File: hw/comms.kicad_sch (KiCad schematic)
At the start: 13 parts, among them J7 CAN IN, J8 CAN OUT, J9 USB-C, SW1 TERM, U6 TCAN3413, U7 USBLC6-2SC6

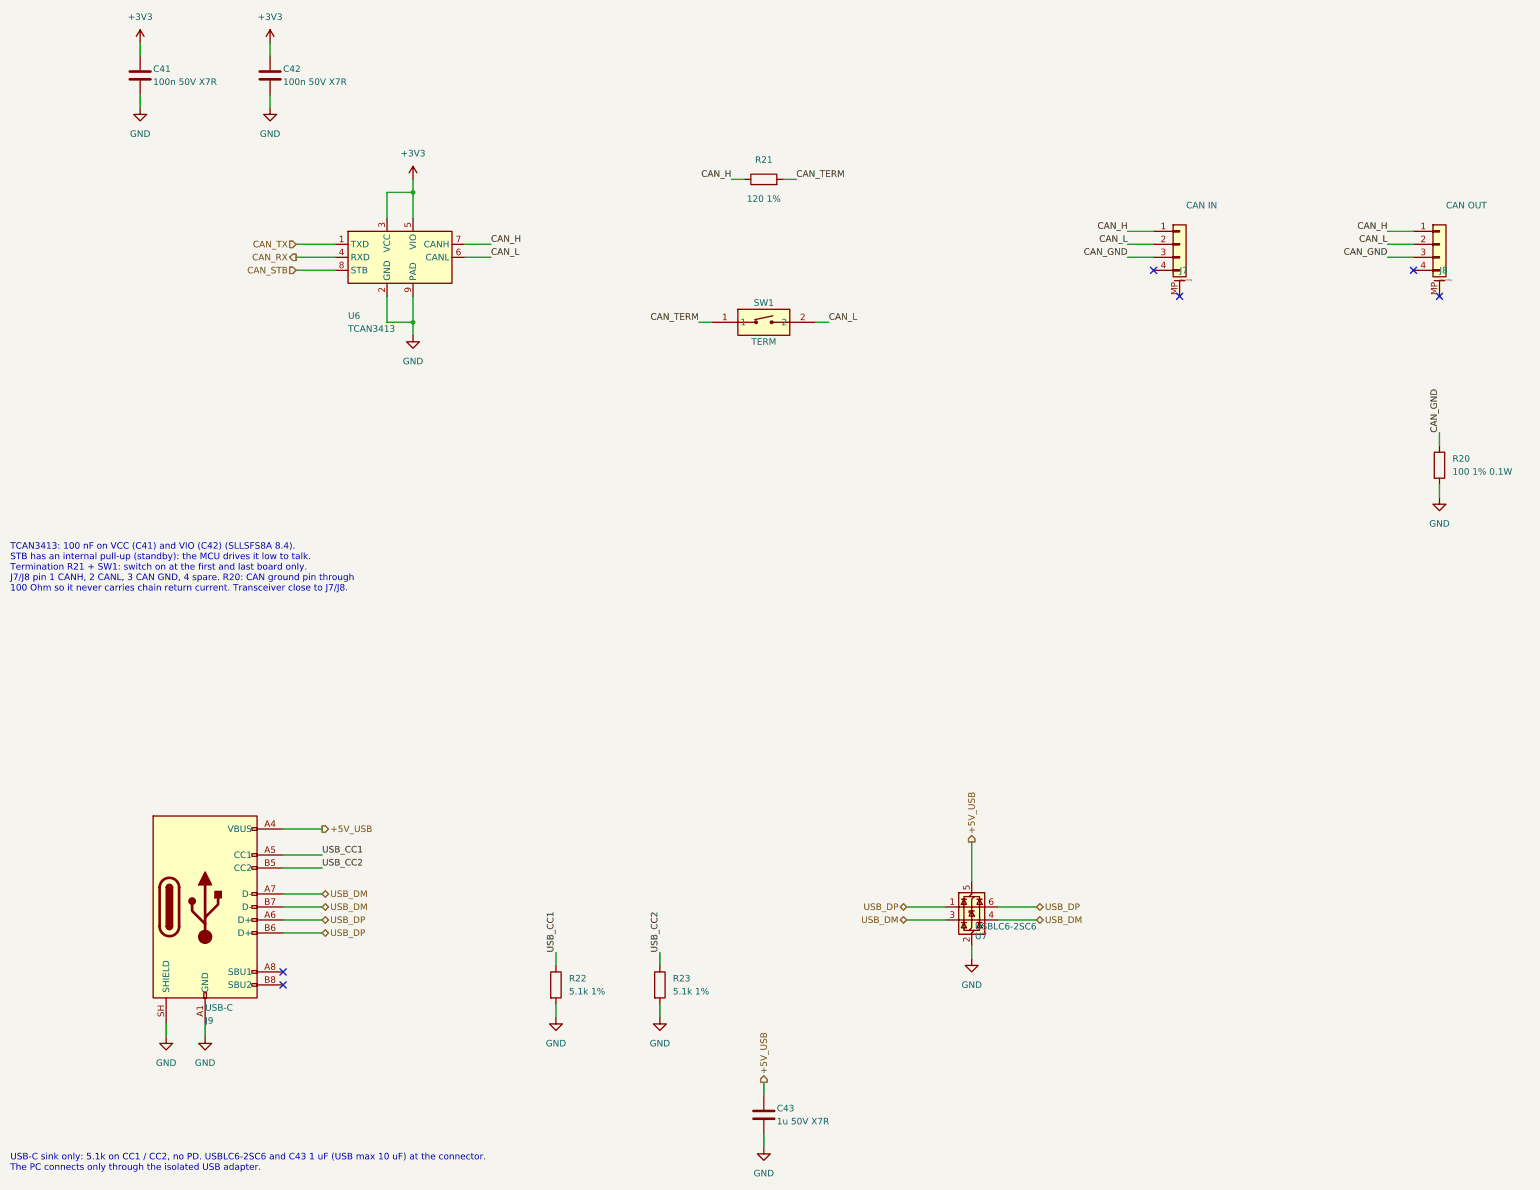
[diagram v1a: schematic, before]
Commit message: Apply schematic review fixes and connector changes
- Remove the RC snubber pads (ringing handled by layout and IDRIVE)
  and renumber R/C references to close the gap.
- CAN connectors: JST-GH 3-pin (CANH, CANL, GND).
- Power connectors: XT30PW-F female for both bus IN and OUT so the
  live side of every link is shrouded; polarity checked on a real
  part (pad 1 GND under the rounded end, pad 2 VBUS under the flat
  end). Male XT30 footprint, model and datasheet removed.
- AS5047P CSn 10k pull-up so encoder inputs never float while the
  MCU is in reset or ROM DFU.
- LM5008A RT 180k -> 240k: on-time stays >= 400 ns at 54 V across
  the TON spread.
- Every BOM line checked in stock against JLCPCB's assembly library.
- Kelvin-tap placement added to the layout rules.

Co-Authored-By: Claude Opus 5.5 <noreply@anthropic.com>
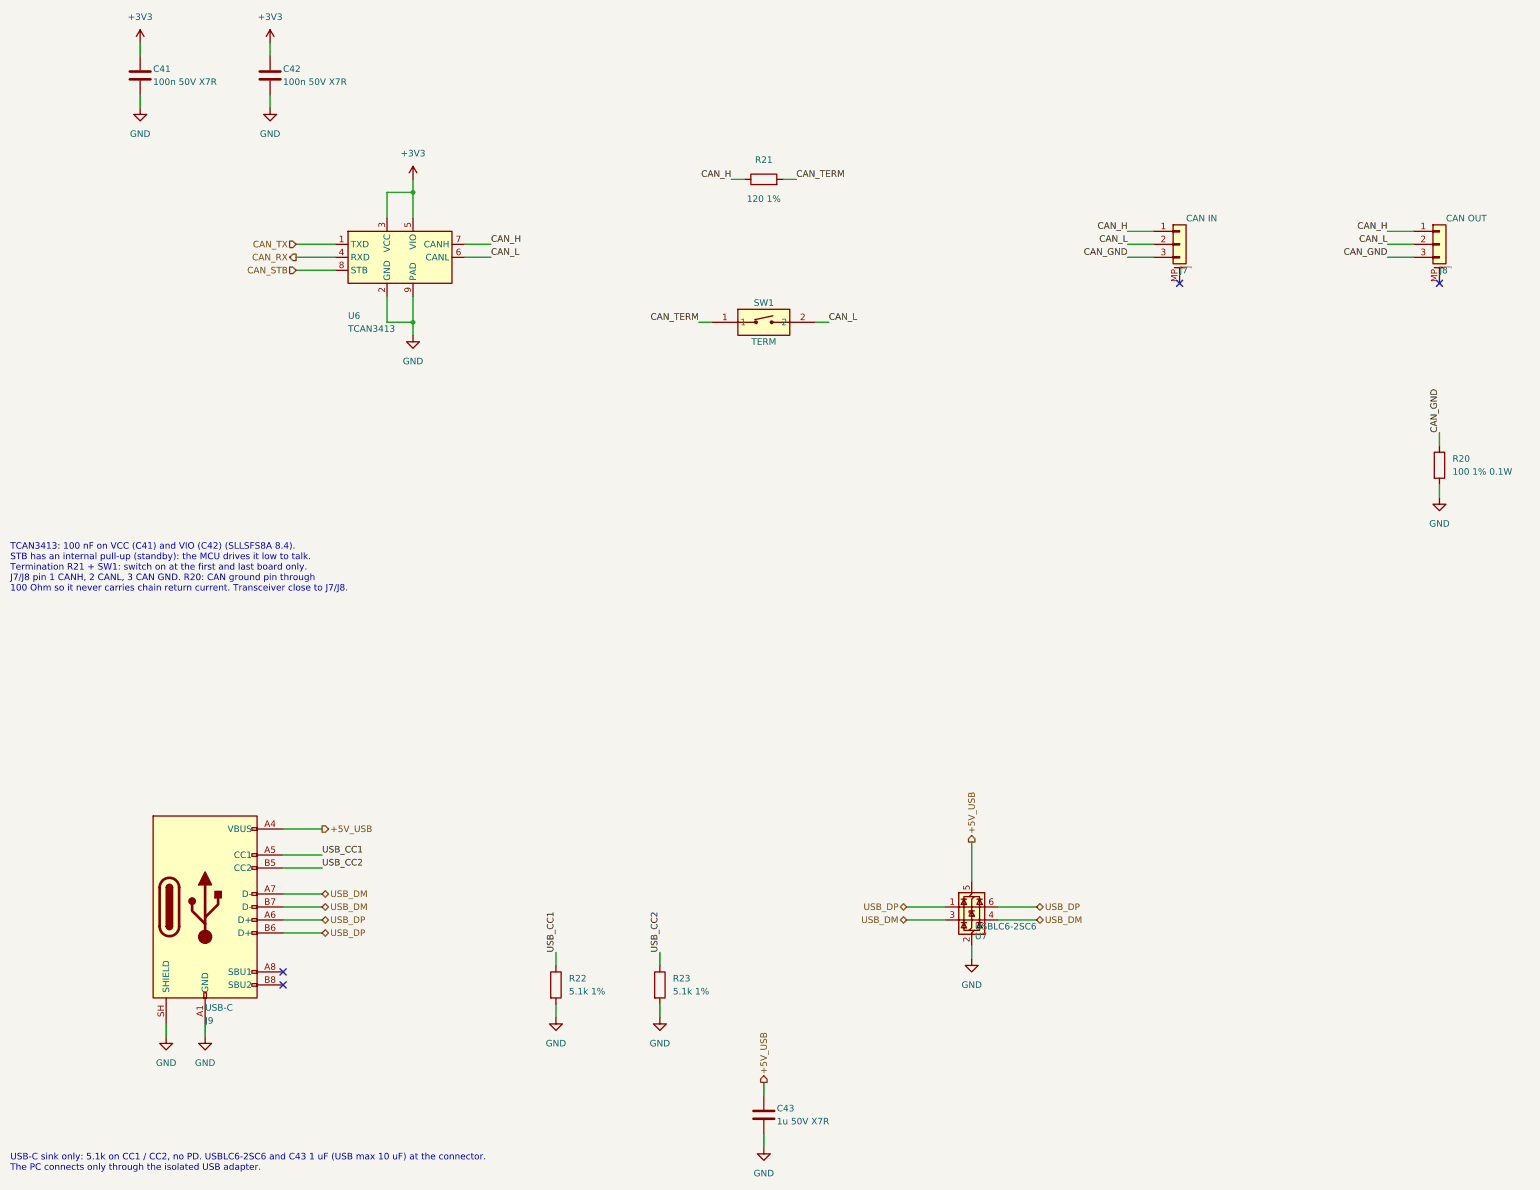
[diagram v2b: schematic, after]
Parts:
- removed J7: CAN IN, Connector_JST:JST_GH_SM04B-GHS-TB_1x04-1MP_P1.25mm_Horizontal, symbol Connector_Generic_MountingPin:Conn_01x04_MountingPin
- removed J8: CAN OUT, Connector_JST:JST_GH_SM04B-GHS-TB_1x04-1MP_P1.25mm_Horizontal, symbol Connector_Generic_MountingPin:Conn_01x04_MountingPin
- added J7: CAN IN, Connector_JST:JST_GH_SM03B-GHS-TB_1x03-1MP_P1.25mm_Horizontal, symbol Connector_Generic_MountingPin:Conn_01x03_MountingPin
- added J8: CAN OUT, Connector_JST:JST_GH_SM03B-GHS-TB_1x03-1MP_P1.25mm_Horizontal, symbol Connector_Generic_MountingPin:Conn_01x03_MountingPin
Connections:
- net CAN_GND: now also J7.3 (Pin_3), J8.3 (Pin_3)
- net CAN_H: now also J7.1 (Pin_1), J8.1 (Pin_1)
- net CAN_L: now also J7.2 (Pin_2), J8.2 (Pin_2)
- no-connect marks 6 -> 4
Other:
- note added: "TCAN3413: 100 nF on VCC (C41) and VIO (C42) (SLLSFS8A 8.4). STB has an internal pull-up (standby): the MCU drives it low to talk. Termination R21 + SW1: switch on at the first and last board only. J7/J8 pin 1 CANH, 2 CANL, 3 CAN GND. R20: CAN ground pin through 100 Ohm so it never carries chain return current. Transceiver close to J7/J8."
- note removed: "TCAN3413: 100 nF on VCC (C41) and VIO (C42) (SLLSFS8A 8.4). STB has an internal pull-up (standby): the MCU drives it low to talk. Termination R21 + SW1: switch on at the first and last board only. J7/J8 pin 1 CANH, 2 CANL, 3 CAN GND, 4 spare. R20: CAN ground pin through 100 Ohm so it never carries chain return current. Transceiver close to J7/J8."
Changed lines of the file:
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@@
 		(instances
 			(project "comms"
-				(path "/23e15ccf-2162-4caa-a05b-71e788486361/49fa0cbe-12ed-4e3b-b7f4-bb953e26e881"
+				(path "/dc3b1c6f-161a-46e4-9985-32c8fd205458/54234469-6ff5-4cf8-9289-b79c93d7bfe3"
 					(reference "U6")
 					(unit 1)
@@
 		(instances
 			(project "comms"
-				(path "/23e15ccf-2162-4caa-a05b-71e788486361/49fa0cbe-12ed-4e3b-b7f4-bb953e26e881"
+				(path "/dc3b1c6f-161a-46e4-9985-32c8fd205458/54234469-6ff5-4cf8-9289-b79c93d7bfe3"
 					(reference "#PWRCOM01")
 					(unit 1)
@@
 		(instances
 			(project "comms"
-				(path "/23e15ccf-2162-4caa-a05b-71e788486361/49fa0cbe-12ed-4e3b-b7f4-bb953e26e881"
+				(path "/dc3b1c6f-161a-46e4-9985-32c8fd205458/54234469-6ff5-4cf8-9289-b79c93d7bfe3"
 					(reference "#PWRCOM02")
 					(unit 1)
@@
 		(instances
 			(project "comms"
-				(path "/23e15ccf-2162-4caa-a05b-71e788486361/49fa0cbe-12ed-4e3b-b7f4-bb953e26e881"
+				(path "/dc3b1c6f-161a-46e4-9985-32c8fd205458/54234469-6ff5-4cf8-9289-b79c93d7bfe3"
 					(reference "C41")
 					(unit 1)
@@
 		(instances
 			(project "comms"
-				(path "/23e15ccf-2162-4caa-a05b-71e788486361/49fa0cbe-12ed-4e3b-b7f4-bb953e26e881"
+				(path "/dc3b1c6f-161a-46e4-9985-32c8fd205458/54234469-6ff5-4cf8-9289-b79c93d7bfe3"
 					(reference "#PWRCOM03")
 					(unit 1)
@@
 		(instances
 			(project "comms"
-				(path "/23e15ccf-2162-4caa-a05b-71e788486361/49fa0cbe-12ed-4e3b-b7f4-bb953e26e881"
+				(path "/dc3b1c6f-161a-46e4-9985-32c8fd205458/54234469-6ff5-4cf8-9289-b79c93d7bfe3"
 					(reference "#PWRCOM04")
 					(unit 1)
@@
 		(instances
 			(project "comms"
-				(path "/23e15ccf-2162-4caa-a05b-71e788486361/49fa0cbe-12ed-4e3b-b7f4-bb953e26e881"
+				(path "/dc3b1c6f-161a-46e4-9985-32c8fd205458/54234469-6ff5-4cf8-9289-b79c93d7bfe3"
 					(reference "C42")
 					(unit 1)
@@
 		(instances
 			(project "comms"
-				(path "/23e15ccf-2162-4caa-a05b-71e788486361/49fa0cbe-12ed-4e3b-b7f4-bb953e26e881"
+				(path "/dc3b1c6f-161a-46e4-9985-32c8fd205458/54234469-6ff5-4cf8-9289-b79c93d7bfe3"
 					(reference "#PWRCOM05")
 					(unit 1)
@@
 		(instances
 			(project "comms"
-				(path "/23e15ccf-2162-4caa-a05b-71e788486361/49fa0cbe-12ed-4e3b-b7f4-bb953e26e881"
+				(path "/dc3b1c6f-161a-46e4-9985-32c8fd205458/54234469-6ff5-4cf8-9289-b79c93d7bfe3"
 					(reference "#PWRCOM06")
 					(unit 1)
@@
 		(instances
 			(project "comms"
-				(path "/23e15ccf-2162-4caa-a05b-71e788486361/49fa0cbe-12ed-4e3b-b7f4-bb953e26e881"
+				(path "/dc3b1c6f-161a-46e4-9985-32c8fd205458/54234469-6ff5-4cf8-9289-b79c93d7bfe3"
 					(reference "R21")
 					(unit 1)
@@
 		(instances
 			(project "comms"
-				(path "/23e15ccf-2162-4caa-a05b-71e788486361/49fa0cbe-12ed-4e3b-b7f4-bb953e26e881"
+				(path "/dc3b1c6f-161a-46e4-9985-32c8fd205458/54234469-6ff5-4cf8-9289-b79c93d7bfe3"
 					(reference "SW1")
 					(unit 1)
@@
 	)
 	(symbol
-		(lib_id "Connector_Generic_MountingPin:Conn_01x04_MountingPin")
+		(lib_id "Connector_Generic_MountingPin:Conn_01x03_MountingPin")
 		(at 254 83.82 0)
 		(unit 1)
@@
 		)
 		(property "Value" "CAN IN"
-			(at 255.27 76.2 0.0000)
-			(effects
-				(font
-					(size 1.27 1.27)
-				)
-				(justify left)
-			)
-		)
-		(property "Footprint" "Connector_JST:JST_GH_SM04B-GHS-TB_1x04-1MP_P1.25mm_Horizontal"
+			(at 255.27 78.74 0.0000)
+			(effects
+				(font
+					(size 1.27 1.27)
+				)
+				(justify left)
+			)
+		)
+		(property "Footprint" "Connector_JST:JST_GH_SM03B-GHS-TB_1x03-1MP_P1.25mm_Horizontal"
 			(at 254 83.82 0.0000)
 			(effects
@@
 			)
 		)
-		(property "LCSC" "C189895"
+		(property "LCSC" "C514175"
 			(at 256.54 88.8999 0)
 			(hide yes)
@@
 			)
 		)
-		(property "MPN" "SM04B-GHS-TB(LF)(SN)"
+		(property "MPN" "SM03B-GHS-TB(LF)(SN)"
 			(at 256.54 88.8999 0)
 			(hide yes)
@@
 		(pin "3"
 		)
-		(pin "4"
-		)
 		(pin "MP"
 		)
 		(instances
 			(project "comms"
-				(path "/23e15ccf-2162-4caa-a05b-71e788486361/49fa0cbe-12ed-4e3b-b7f4-bb953e26e881"
+				(path "/dc3b1c6f-161a-46e4-9985-32c8fd205458/54234469-6ff5-4cf8-9289-b79c93d7bfe3"
 					(reference "J7")
 					(unit 1)
@@
 	)
 	(symbol
-		(lib_id "Connector_Generic_MountingPin:Conn_01x04_MountingPin")
+		(lib_id "Connector_Generic_MountingPin:Conn_01x03_MountingPin")
 		(at 304.8 83.82 0)
 		(unit 1)
@@
 		)
 		(property "Value" "CAN OUT"
-			(at 306.07 76.2 0.0000)
-			(effects
-				(font
-					(size 1.27 1.27)
-				)
-				(justify left)
-			)
-		)
-		(property "Footprint" "Connector_JST:JST_GH_SM04B-GHS-TB_1x04-1MP_P1.25mm_Horizontal"
+			(at 306.07 78.74 0.0000)
+			(effects
+				(font
+					(size 1.27 1.27)
+				)
+				(justify left)
+			)
+		)
+		(property "Footprint" "Connector_JST:JST_GH_SM03B-GHS-TB_1x03-1MP_P1.25mm_Horizontal"
 			(at 304.8 83.82 0.0000)
 			(effects
@@
 			)
 		)
-		(property "LCSC" "C189895"
+		(property "LCSC" "C514175"
 			(at 307.34 88.8999 0)
 			(hide yes)
@@
 			)
 		)
-		(property "MPN" "SM04B-GHS-TB(LF)(SN)"
+		(property "MPN" "SM03B-GHS-TB(LF)(SN)"
 			(at 307.34 88.8999 0)
 			(hide yes)
@@
 		(pin "3"
 		)
-		(pin "4"
-		)
 		(pin "MP"
 		)
 		(instances
 			(project "comms"
-				(path "/23e15ccf-2162-4caa-a05b-71e788486361/49fa0cbe-12ed-4e3b-b7f4-bb953e26e881"
+				(path "/dc3b1c6f-161a-46e4-9985-32c8fd205458/54234469-6ff5-4cf8-9289-b79c93d7bfe3"
 					(reference "J8")
 					(unit 1)
@@
 		(instances
 			(project "comms"
-				(path "/23e15ccf-2162-4caa-a05b-71e788486361/49fa0cbe-12ed-4e3b-b7f4-bb953e26e881"
+				(path "/dc3b1c6f-161a-46e4-9985-32c8fd205458/54234469-6ff5-4cf8-9289-b79c93d7bfe3"
 					(reference "R20")
 					(unit 1)
@@
 		(instances
 			(project "comms"
-				(path "/23e15ccf-2162-4caa-a05b-71e788486361/49fa0cbe-12ed-4e3b-b7f4-bb953e26e881"
+				(path "/dc3b1c6f-161a-46e4-9985-32c8fd205458/54234469-6ff5-4cf8-9289-b79c93d7bfe3"
 					(reference "#PWRCOM07")
 					(unit 1)
@@
 		(instances
 			(project "comms"
-				(path "/23e15ccf-2162-4caa-a05b-71e788486361/49fa0cbe-12ed-4e3b-b7f4-bb953e26e881"
+				(path "/dc3b1c6f-161a-46e4-9985-32c8fd205458/54234469-6ff5-4cf8-9289-b79c93d7bfe3"
 					(reference "J9")
 					(unit 1)
@@
 		(instances
 			(project "comms"
-				(path "/23e15ccf-2162-4caa-a05b-71e788486361/49fa0cbe-12ed-4e3b-b7f4-bb953e26e881"
+				(path "/dc3b1c6f-161a-46e4-9985-32c8fd205458/54234469-6ff5-4cf8-9289-b79c93d7bfe3"
 					(reference "#PWRCOM08")
 					(unit 1)
@@
 		(instances
 			(project "comms"
-				(path "/23e15ccf-2162-4caa-a05b-71e788486361/49fa0cbe-12ed-4e3b-b7f4-bb953e26e881"
+				(path "/dc3b1c6f-161a-46e4-9985-32c8fd205458/54234469-6ff5-4cf8-9289-b79c93d7bfe3"
 					(reference "#PWRCOM09")
 					(unit 1)
@@
 		(instances
 			(project "comms"
-				(path "/23e15ccf-2162-4caa-a05b-71e788486361/49fa0cbe-12ed-4e3b-b7f4-bb953e26e881"
+				(path "/dc3b1c6f-161a-46e4-9985-32c8fd205458/54234469-6ff5-4cf8-9289-b79c93d7bfe3"
 					(reference "C43")
 					(unit 1)
@@
 		(instances
 			(project "comms"
-				(path "/23e15ccf-2162-4caa-a05b-71e788486361/49fa0cbe-12ed-4e3b-b7f4-bb953e26e881"
+				(path "/dc3b1c6f-161a-46e4-9985-32c8fd205458/54234469-6ff5-4cf8-9289-b79c93d7bfe3"
 					(reference "#PWRCOM10")
 					(unit 1)
@@
 		(instances
 			(project "comms"
-				(path "/23e15ccf-2162-4caa-a05b-71e788486361/49fa0cbe-12ed-4e3b-b7f4-bb953e26e881"
+				(path "/dc3b1c6f-161a-46e4-9985-32c8fd205458/54234469-6ff5-4cf8-9289-b79c93d7bfe3"
 					(reference "R22")
 					(unit 1)
@@
 		(instances
 			(project "comms"
-				(path "/23e15ccf-2162-4caa-a05b-71e788486361/49fa0cbe-12ed-4e3b-b7f4-bb953e26e881"
+				(path "/dc3b1c6f-161a-46e4-9985-32c8fd205458/54234469-6ff5-4cf8-9289-b79c93d7bfe3"
 					(reference "#PWRCOM11")
 					(unit 1)
@@
 		(instances
 			(project "comms"
-				(path "/23e15ccf-2162-4caa-a05b-71e788486361/49fa0cbe-12ed-4e3b-b7f4-bb953e26e881"
+				(path "/dc3b1c6f-161a-46e4-9985-32c8fd205458/54234469-6ff5-4cf8-9289-b79c93d7bfe3"
 					(reference "R23")
 					(unit 1)
@@
 		(instances
 			(project "comms"
-				(path "/23e15ccf-2162-4caa-a05b-71e788486361/49fa0cbe-12ed-4e3b-b7f4-bb953e26e881"
+				(path "/dc3b1c6f-161a-46e4-9985-32c8fd205458/54234469-6ff5-4cf8-9289-b79c93d7bfe3"
 					(reference "#PWRCOM12")
 					(unit 1)
@@
 		(instances
 			(project "comms"
-				(path "/23e15ccf-2162-4caa-a05b-71e788486361/49fa0cbe-12ed-4e3b-b7f4-bb953e26e881"
+				(path "/dc3b1c6f-161a-46e4-9985-32c8fd205458/54234469-6ff5-4cf8-9289-b79c93d7bfe3"
 					(reference "U7")
 					(unit 1)
@@
 		(instances
 			(project "comms"
-				(path "/23e15ccf-2162-4caa-a05b-71e788486361/49fa0cbe-12ed-4e3b-b7f4-bb953e26e881"
+				(path "/dc3b1c6f-161a-46e4-9985-32c8fd205458/54234469-6ff5-4cf8-9289-b79c93d7bfe3"
 					(reference "#PWRCOM13")
 					(unit 1)
@@
 	)
 	(no_connect
-		(at 248.92 88.9)
+		(at 254 91.44)
 	)
 	(no_connect
-		(at 254 93.98)
-	)
-	(no_connect
-		(at 299.72 88.9)
-	)
-	(no_connect
-		(at 304.8 93.98)
+		(at 304.8 91.44)
 	)
 	(no_connect
@@
 		(at 78.74 228.6)
 	)
-	(text "TCAN3413: 100 nF on VCC (C41) and VIO (C42) (SLLSFS8A 8.4).\nSTB has an internal pull-up (standby): the MCU drives it low to talk.\nTermination R21 + SW1: switch on at the first and last board only.\nJ7/J8 pin 1 CANH, 2 CANL, 3 CAN GND, 4 spare. R20: CAN ground pin through\n100 Ohm so it never carries chain return current. Transceiver close to J7/J8."
+	(text "TCAN3413: 100 nF on VCC (C41) and VIO (C42) (SLLSFS8A 8.4).\nSTB has an internal pull-up (standby): the MCU drives it low to talk.\nTermination R21 + SW1: switch on at the first and last board only.\nJ7/J8 pin 1 CANH, 2 CANL, 3 CAN GND. R20: CAN ground pin through\n100 Ohm so it never carries chain return current. Transceiver close to J7/J8."
 		(exclude_from_sim no)
 		(at 25.4 142.24 0.0000)
